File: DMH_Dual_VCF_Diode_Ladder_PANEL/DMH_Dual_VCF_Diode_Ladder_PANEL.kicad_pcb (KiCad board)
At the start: 2 copper layers, 100 x 200 mm, 20 parts, among them J0 Panel_GND_Solder_Wire_Pad

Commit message: Finished panel
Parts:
- added H20: BP, SynthStuff:Toggle_Switch_Cutout, F.Cu at (62.5, 190.2)
- added H21: Drive, SynthStuff:Pot_Cutout_Small, F.Cu at (120.0, 106.0)
- added H22: CV 1 Amt, SynthStuff:Pot_Cutout_Tiny, F.Cu at (115.0, 140.2)
- added H23: Bus CV, SynthStuff:Toggle_Switch_Cutout, F.Cu at (137.5, 140.2)
- added H24: LP, SynthStuff:Toggle_Switch_Cutout, F.Cu at (115.0, 165.2)
- added H25: CV 2, SynthStuff:Jack_6.35mm_Cutout_v3, F.Cu at (137.5, 208.8)
- added H26: HP, SynthStuff:Toggle_Switch_Cutout, F.Cu at (85.0, 165.2)
- added H27: Cutoff, SynthStuff:Pot_Cutout_Large_v2, F.Cu at (137.5, 64.2)
- added H28: (Bus) CV 2 Amt, SynthStuff:Pot_Cutout_Tiny, F.Cu at (137.5, 165.2)
- added H29: CV 3, SynthStuff:Jack_6.35mm_Cutout_v3, F.Cu at (160.0, 208.8)
- added H30: Output, SynthStuff:Jack_6.35mm_Cutout_Output_v6, F.Cu at (160.0, 190.2)
- added H31: Resonance, SynthStuff:Pot_Cutout_Small, F.Cu at (155.0, 106.0)
- added H32: CV 3 Amt, SynthStuff:Pot_Cutout_Tiny, F.Cu at (160.0, 140.2)
- added H33: Link, SynthStuff:Toggle_Switch_Cutout, F.Cu at (100.0, 64.2)
- added H34: BP, SynthStuff:Toggle_Switch_Cutout, F.Cu at (137.5, 190.2)
- added H35: HP, SynthStuff:Toggle_Switch_Cutout, F.Cu at (160.0, 165.2)
- added H36: MountingHole_Rails, SynthStuff:MountingHole_Rails, F.Cu at (71.5, 33.5)
- added H37: MountingHole_Rails, SynthStuff:MountingHole_Rails, F.Cu at (71.5, 226.5)
- added H38: MountingHole_Rails, SynthStuff:MountingHole_Rails, F.Cu at (128.5, 33.5)
- added H39: MountingHole_Rails, SynthStuff:MountingHole_Rails, F.Cu at (128.5, 226.5)
- added H40: LED A, SynthStuff:MountingHole_LED_3mm, F.Cu at (62.5, 91.0)
- added H41: LED Link, SynthStuff:MountingHole_LED_3mm, F.Cu at (100.0, 85.0)
- added H42: LED B, SynthStuff:MountingHole_LED_3mm, F.Cu at (137.5, 91.0)
- H10, H11: footprint SynthStuff:Pot_Cutout_Medium -> SynthStuff:Pot_Cutout_Small
- H12: value CV 1 Amount -> CV 1 Amt
- H13: value CV 3 Amount -> CV 3 Amt
- H15: value BP -> CV 1; footprint SynthStuff:Toggle_Switch_Cutout -> SynthStuff:Jack_6.35mm_Cutout_v3
- H16: value HP -> Input; footprint SynthStuff:Toggle_Switch_Cutout -> SynthStuff:Jack_6.35mm_Cutout_v3
- H17: value (Bus) CV 2 Amount -> (Bus) CV 2 Amt
- H9: footprint SynthStuff:Pot_Cutout_Huge_v2 -> SynthStuff:Pot_Cutout_Large_v2
- moved H8 55.7 mm to (85.0, 190.2)
- moved H13 49.9 mm to (85.0, 140.2)
- moved H11 48.7 mm to (80.0, 106.0)
- moved H6 41.2 mm to (40.0, 208.8)
- moved H14 39.4 mm to (40.0, 165.2)
- moved H9 39.1 mm to (62.5, 64.2)
- moved H12 37.9 mm to (40.0, 140.2)
- moved H17 37.5 mm to (62.5, 165.2)
- moved H19 37.5 mm to (62.5, 140.2)
- moved H18 37.5 mm to (62.5, 208.8)
- moved H10 35.2 mm to (45.0, 106.0)
- moved H7 33.8 mm to (85.0, 208.8)
- moved H5 29.1 mm to (40.0, 190.2)
- moved H1 25.0 mm to (28.5, 33.5)
- moved H2 25.0 mm to (171.5, 33.5)
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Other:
- board size 100 x 200 mm -> 150 x 200 mm
- board text added: "A"
- board text added: "B"
- board text added: "Unlink"
- board text removed: "(Bus) CV 2"
- board text removed: "CV 1"
- board text removed: "CV 3"

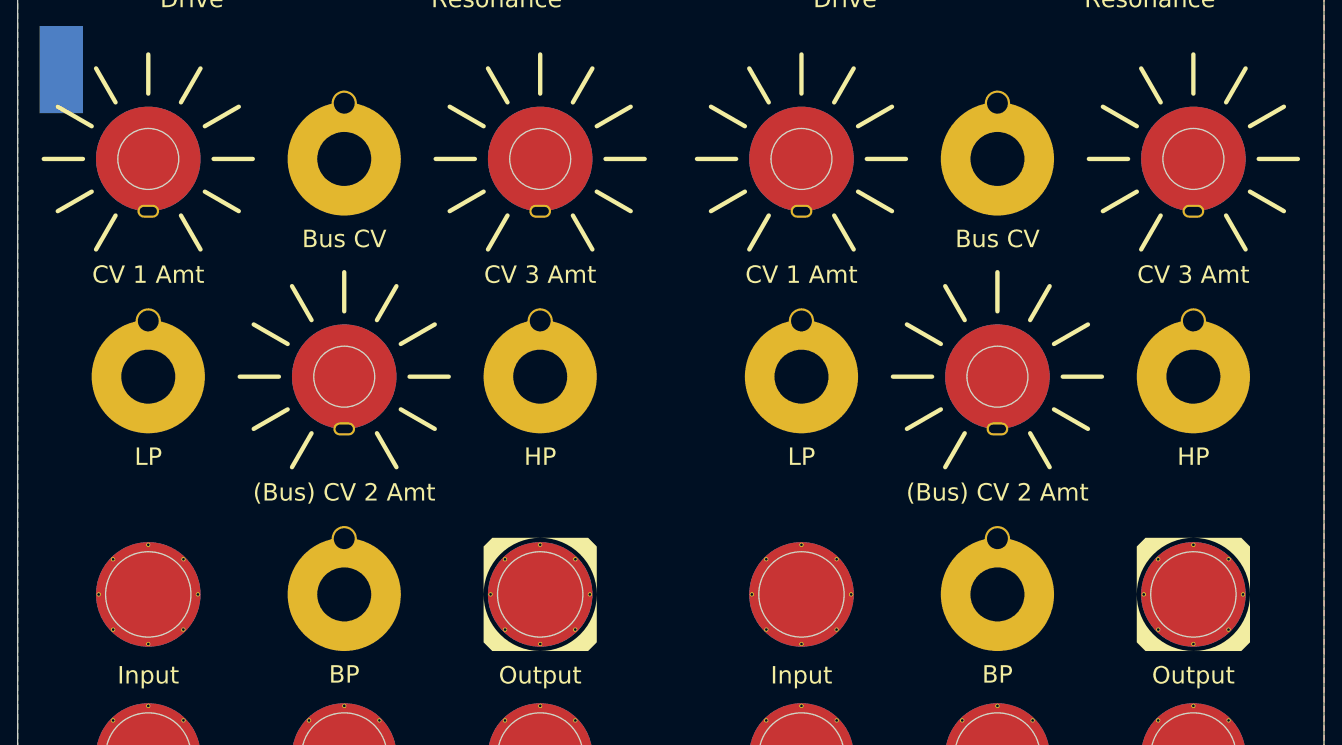
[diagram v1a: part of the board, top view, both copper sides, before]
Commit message: Changed line art
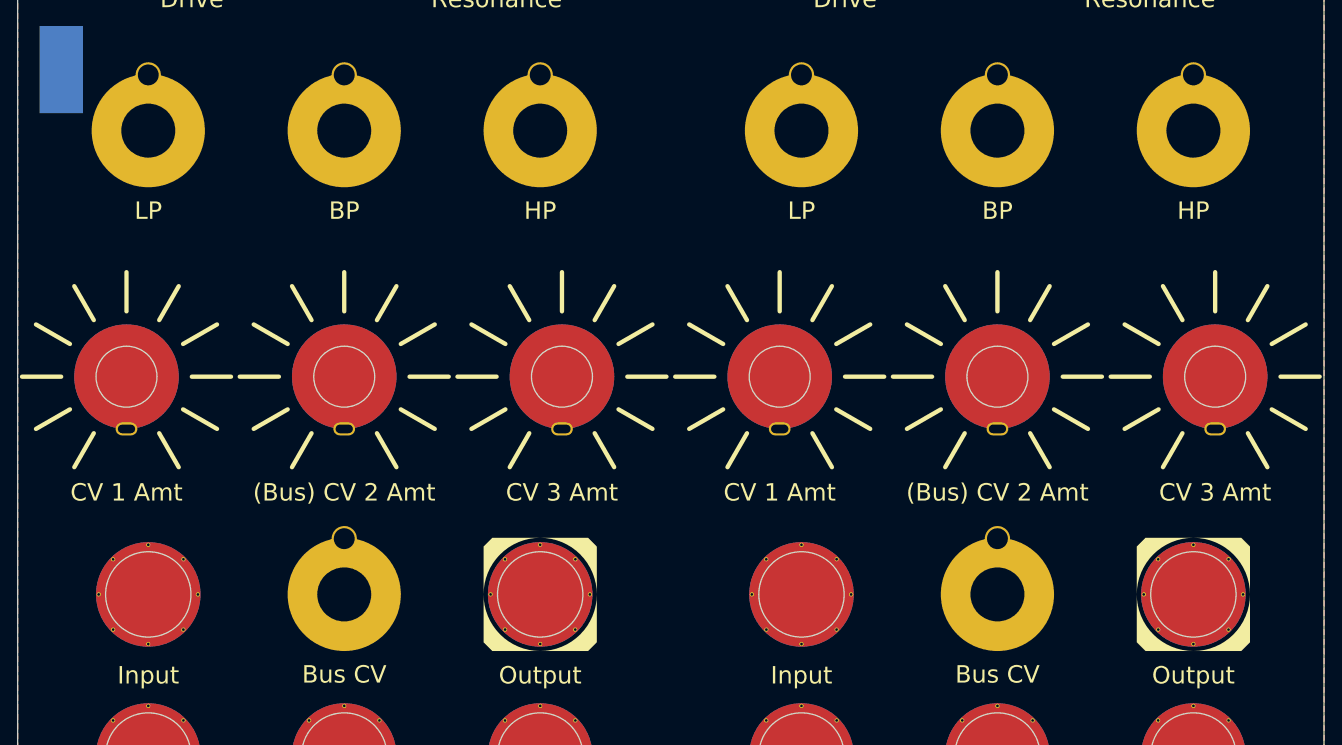
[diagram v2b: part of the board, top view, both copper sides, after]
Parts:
- moved H20 53.2 mm to (62.5, 137.0)
- moved H34 53.2 mm to (137.5, 137.0)
- moved H19 50.0 mm to (62.5, 190.2)
- moved H23 50.0 mm to (137.5, 190.2)
- moved H14 28.2 mm to (40.0, 137.0)
- moved H24 28.2 mm to (115.0, 137.0)
- moved H26 28.2 mm to (85.0, 137.0)
- moved H35 28.2 mm to (160.0, 137.0)
- moved H12 25.1 mm to (37.5, 165.2)
- moved H13 25.1 mm to (87.5, 165.2)
- moved H22 25.1 mm to (112.5, 165.2)
- moved H32 25.1 mm to (162.5, 165.2)

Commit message: Changed from unlink to split
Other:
- board text added: "Split"
- board text removed: "Unlink"
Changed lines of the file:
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@@
 		)
 	)
-	(gr_text "Unlink"
+	(gr_text "Split"
 		(at 100 54.25 0)
 		(layer "F.SilkS")
@@
 			)
 		)
-		(render_cache "Unlink" 0
+		(render_cache "Split" 0
 			(polygon
 				(pts
-					(xy 95.092184 55.08) (xy 95.218482 55.075158) (xy 95.33008 55.060435) (xy 95.427474 55.03553) (xy 95.536098 54.985967)
-					(xy 95.621535 54.917062) (xy 95.684965 54.828104) (xy 95.727566 54.718383) (xy 95.746558 54.62204)
-					(xy 95.754995 54.51332) (xy 95.755548 54.474277) (xy 95.755548 53.172951) (xy 95.246057 53.172951)
-					(xy 95.246057 54.417613) (xy 95.224119 54.520353) (xy 95.140956 54.585156) (xy 95.058478 54.59591)
-					(xy 94.271528 54.59591) (xy 94.173423 54.578466) (xy 94.102958 54.503731) (xy 94.089323 54.417613)
-					(xy 94.089323 53.172951) (xy 93.579832 53.172951) (xy 93.579832 54.474277) (xy 93.584861 54.58719)
-					(xy 93.600282 54.687626) (xy 93.637873 54.802648) (xy 93.696011 54.89673) (xy 93.775882 54.970582)
-					(xy 93.878671 55.024914) (xy 94.005562 55.060435) (xy 94.117261 55.075158) (xy 94.243684 55.08)
+					(xy 97.176064 53.172951) (xy 95.787299 53.172951) (xy 95.676872 53.177769) (xy 95.563281 53.195578)
+					(xy 95.467851 53.22534) (xy 95.375964 53.273518) (xy 95.291486 53.343921) (xy 95.223693 53.428124)
+					(xy 95.172662 53.52405) (xy 95.140498 53.629685) (xy 95.129489 53.728496) (xy 95.129309 53.743014)
+					(xy 95.13755 53.847156) (xy 95.161578 53.943628) (xy 95.207031 54.043467) (xy 95.270184 54.131056)
+					(xy 95.288555 54.1509) (xy 95.373697 54.221226) (xy 95.466442 54.26926) (xy 95.562594 54.298888)
+					(xy 95.67671 54.316595) (xy 95.787299 54.321381) (xy 96.557153 54.321381) (xy 96.657225 54.337863)
+					(xy 96.691486 54.363391) (xy 96.730405 54.455757) (xy 96.730565 54.463042) (xy 96.69979 54.548527)
+					(xy 96.609115 54.592834) (xy 96.557153 54.59591) (xy 95.179623 54.59591) (xy 95.179623 55.08) (xy 96.647034 55.08)
+					(xy 96.746704 55.074603) (xy 96.853116 55.054543) (xy 96.946048 55.020774) (xy 97.038723 54.965625)
+					(xy 97.1159 54.895294) (xy 97.12575 54.884117) (xy 97.184055 54.803204) (xy 97.228027 54.713086)
+					(xy 97.255786 54.616282) (xy 97.265457 54.51531) (xy 97.254267 54.407141) (xy 97.222104 54.304284)
+					(xy 97.171072 54.209487) (xy 97.10328 54.125498) (xy 97.01942 54.055095) (xy 96.93099 54.006917)
+					(xy 96.826743 53.973324) (xy 96.723519 53.957627) (xy 96.647034 53.954528) (xy 95.815143 53.954528)
+					(xy 95.719141 53.935281) (xy 95.705722 53.924731) (xy 95.659727 53.838157) (xy 95.658339 53.817752)
+					(xy 95.688586 53.723699) (xy 95.697418 53.713217) (xy 95.788268 53.675679) (xy 95.815143 53.674626)
+					(xy 97.176064 53.674626)
 				)
 			)
 			(polygon
 				(pts
-					(xy 98.373342 53.172951) (xy 97.877529 53.172951) (xy 97.877529 54.405889) (xy 97.838451 54.456692)
-					(xy 97.790579 54.434221) (xy 96.866852 53.319986) (xy 96.78967 53.245882) (xy 96.697619 53.18742)
-					(xy 96.594886 53.15382) (xy 96.490832 53.142258) (xy 96.45799 53.141688) (xy 96.344052 53.150867)
-					(xy 96.243034 53.179625) (xy 96.157552 53.229795) (xy 96.090223 53.303213) (xy 96.043663 53.401711)
-					(xy 96.023127 53.499799) (xy 96.018353 53.585233) (xy 96.018353 55.08) (xy 96.516608 55.08) (xy 96.516608 53.795771)
-					(xy 96.563991 53.742037) (xy 96.608932 53.767438) (xy 97.647941 54.971067) (xy 97.730959 55.039618)
-					(xy 97.829858 55.085007) (xy 97.931944 55.106487) (xy 98.017725 55.111263) (xy 98.11911 55.098241)
-					(xy 98.211388 55.057991) (xy 98.28834 54.988735) (xy 98.343743 54.888696) (xy 98.368964 54.780533)
-					(xy 98.373342 54.704354)
+					(xy 98.942736 53.176577) (xy 99.051652 53.190919) (xy 99.148535 53.215493) (xy 99.250471 53.257482)
+					(xy 99.338586 53.311939) (xy 99.414794 53.377627) (xy 99.438888 53.402857) (xy 99.503256 53.485231)
+					(xy 99.555001 53.576518) (xy 99.593158 53.675288) (xy 99.616761 53.780112) (xy 99.624843 53.88956)
+					(xy 99.621996 53.954337) (xy 99.603818 54.064098) (xy 99.569897 54.16799) (xy 99.52146 54.26451)
+					(xy 99.459735 54.352156) (xy 99.434796 54.380457) (xy 99.350474 54.457119) (xy 99.268556 54.510535)
+					(xy 99.175199 54.55329) (xy 99.069612 54.584309) (xy 98.950999 54.60252) (xy 98.846197 54.607145)
+					(xy 97.975715 54.607145) (xy 97.975715 55.08) (xy 97.468667 55.08) (xy 97.468667 53.71517) (xy 97.975715 53.71517)
+					(xy 97.975715 54.142107) (xy 98.857432 54.142107) (xy 98.897369 54.140503) (xy 98.999769 54.114427)
+					(xy 99.076273 54.049295) (xy 99.100786 54.007389) (xy 99.120725 53.910076) (xy 99.114937 53.853113)
+					(xy 99.073342 53.761577) (xy 99.047194 53.734143) (xy 98.955253 53.686226) (xy 98.857432 53.674626)
+					(xy 98.011863 53.674626) (xy 97.975715 53.71517) (xy 97.468667 53.71517) (xy 97.468667 53.290676)
+					(xy 97.496057 53.206306) (xy 97.591765 53.172951) (xy 98.846197 53.172951)
 				)
 			)
 			(polygon
 				(pts
-					(xy 100.631612 55.08) (xy 100.631612 54.59591) (xy 99.318074 54.59591) (xy 99.220873 54.58182)
-					(xy 99.157812 54.501526) (xy 99.150035 54.414682) (xy 99.150035 53.172951) (xy 98.640544 53.172951)
-					(xy 98.640544 54.463042) (xy 98.64467 54.573638) (xy 98.657581 54.673255) (xy 98.689843 54.78904)
-					(xy 98.741038 54.885399) (xy 98.813062 54.962383) (xy 98.907809 55.020045) (xy 99.027174 55.058435)
-					(xy 99.133993 55.074612) (xy 99.256524 55.08)
+					(xy 101.808862 55.08) (xy 101.808862 54.59591) (xy 100.495324 54.59591) (xy 100.398124 54.58182)
+					(xy 100.335063 54.501526) (xy 100.327285 54.414682) (xy 100.327285 53.172951) (xy 99.817795 53.172951)
+					(xy 99.817795 54.463042) (xy 99.821921 54.573638) (xy 99.834832 54.673255) (xy 99.867093 54.78904)
+					(xy 99.918289 54.885399) (xy 99.990312 54.962383) (xy 100.085059 55.020045) (xy 100.204424 55.058435)
+					(xy 100.311243 55.074612) (xy 100.433775 55.08)
 				)
 			)
 			(polygon
 				(pts
-					(xy 100.829448 53.172951) (xy 100.829448 55.08) (xy 101.338939 55.08) (xy 101.338939 53.172951)
+					(xy 102.006699 53.172951) (xy 102.006699 55.08) (xy 102.51619 55.08) (xy 102.51619 53.172951)
 				)
 			)
 			(polygon
 				(pts
-					(xy 103.971388 53.172951) (xy 103.475575 53.172951) (xy 103.475575 54.405889) (xy 103.436497 54.456692)
-					(xy 103.388625 54.434221) (xy 102.464899 53.319986) (xy 102.387716 53.245882) (xy 102.295665 53.18742)
-					(xy 102.192932 53.15382) (xy 102.088878 53.142258) (xy 102.056036 53.141688) (xy 101.942098 53.150867)
-					(xy 101.84108 53.179625) (xy 101.755598 53.229795) (xy 101.688269 53.303213) (xy 101.641709 53.401711)
-					(xy 101.621173 53.499799) (xy 101.616399 53.585233) (xy 101.616399 55.08) (xy 102.114654 55.08)
-					(xy 102.114654 53.795771) (xy 102.162037 53.742037) (xy 102.206978 53.767438) (xy 103.245987 54.971067)
-					(xy 103.329005 55.039618) (xy 103.427904 55.085007) (xy 103.52999 55.106487) (xy 103.615771 55.111263)
-					(xy 103.717156 55.098241) (xy 103.809434 55.057991) (xy 103.886386 54.988735) (xy 103.941789 54.888696)
-					(xy 103.96701 54.780533) (xy 103.971388 54.704354)
+					(xy 102.715003 53.172951) (xy 102.715003 53.674626) (xy 103.546894 53.674626) (xy 103.546894 55.08)
+					(xy 104.056385 55.08) (xy 104.056385 53.674626) (xy 104.885345 53.674626) (xy 104.885345 53.172951)
 				)
 			)
-			(polygon
-				(pts
-					(xy 104.249825 53.172951) (xy 104.249825 55.08) (xy 104.762247 55.08) (xy 104.762247 54.236873)
-					(xy 105.669365 55.001353) (xy 105.742619 55.068277) (xy 105.753384 55.08) (xy 106.50956 55.08)
-					(xy 106.439156 55.011766) (xy 106.436776 55.009658) (xy 105.319609 54.098632) (xy 105.303 54.067369)
-					(xy 105.319609 54.036594) (xy 106.36106 53.223754) (xy 106.411863 53.172951) (xy 105.70307 53.172951)
-					(xy 105.632809 53.245546) (xy 105.624912 53.252086) (xy 104.762247 53.954528) (xy 104.762247 53.172951)
-				)
-			)
